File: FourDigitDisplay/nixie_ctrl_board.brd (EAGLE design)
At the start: 100 x 50 mm, 8 parts, among them Q1 IN-12B, Q2 IN-12B, Q3 IN-12B, Q4 IN-12B

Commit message: IC群を追加して仮置き
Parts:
- added CN1: PIC_CN_H, Connectors:HEADER_6PIN
- added CN2: I2C_IF, PartsForProto:I2C_IF_4PIN
- added R1, R2, R8, R9: 20k, Parts:RESISTOR_0207_300MIL
- added R11, R12, R3, R4: 470, Parts:RESISTOR_0207_300MIL
- added U1, U3: TLP627-2, Parts:DIL08
- added U2, U4: SN74141, Parts:DIL16
- added U5: PIC16F18857-I/SP, Parts:DIL28-3
- moved Q1 1.27 mm to (12.1, 26.7)
- moved Q2 1.27 mm to (37.5, 26.7)
- moved Q3 1.27 mm to (62.9, 26.7)
- moved Q4 1.27 mm to (88.3, 26.7)
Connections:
- new net +24V: R1.2, R2.2, R8.2, R9.2
- new net +5V: U2.5, U4.5
- new net 0V: U1.2, U1.4, U2.12, U3.2, U3.4, U4.12
- new net A1_CTL: R11.1
- new net A2_CTL: R12.1
- new net A3_CTL: R3.1
- new net A4_CTL: R4.1
- new net N$1: R1.1, U1.8
- new net N$11: R8.1, U3.8
- new net N$12: R9.1, U3.6
- new net N$13: R11.2, U3.1
- new net N$14: R12.2, U3.3
- new net N$2: R2.1, U1.6
- new net N$3: R3.2, U1.1
- new net N$4: R4.2, U1.3
- new net PIC_A1: U2.3
- new net PIC_A2: U4.3
- new net PIC_B1: U2.6
- new net PIC_B2: U4.6
- new net PIC_C1: U2.7
- new net PIC_C2: U4.7
- new net PIC_D1: U2.4
- new net PIC_D2: U4.4
- net A_1: now also U3.7
- net A_2: now also U3.5
- net A_3: now also U1.7
- net A_4: now also U1.5
- net K1_0: now also U2.16
- net K1_1: now also U2.15
- net K1_2: now also U2.8
- net K1_3: now also U2.9
- net K1_4: now also U2.13
- net K1_5: now also U2.14
- net K1_6: now also U2.11
- net K1_7: now also U2.10
- net K1_8: now also U2.1
- net K1_9: now also U2.2
- net K2_0: now also U4.16
- net K2_1: now also U4.15
- net K2_2: now also U4.8
- net K2_3: now also U4.9
- net K2_4: now also U4.13
- net K2_5: now also U4.14
- net K2_6: now also U4.11
- net K2_7: now also U4.10
- net K2_8: now also U4.1
- net K2_9: now also U4.2
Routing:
- added copper zone on layer 16, net 0V
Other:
- board size 100 x 50 mm -> 100 x 65 mm

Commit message: 配線の追加
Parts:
- added C1: 0.1uF, Parts:CAP_100MIL
- added CN3, CN4: POWER_IF, PartsForProto:HEADER_2PIN_POWER_IF
- added R5: 10k, Parts:RESISTOR_0207_300MIL
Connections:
- new net N$15: CN1.3, U5.8
- new net N$5: CN2.2, U5.15
- new net N$6: CN2.3, U5.14
- new net N$7: CN1.1, R5.1, U5.1
- new net N$8: CN1.4, U5.28
- new net N$9: CN1.5, U5.27
- net +24V: now also CN3.2
- net +5V: now also C1.1, CN1.2, CN2.4, CN4.2, R5.2, U5.20
- net 0V: now also C1.2, CN2.1, CN3.1, CN4.1, U5.19
- net A1_CTL: now also U5.6
- net A2_CTL: now also U5.7
- net A3_CTL: now also U5.25
- net A4_CTL: now also U5.26
- net K1_D: now also U5.11
- net K2_D: now also U5.12
- net PIC_A1: now also U5.2
- net PIC_A2: now also U5.21
- net PIC_B1: now also U5.3
- net PIC_B2: now also U5.22
- net PIC_C1: now also U5.4
- net PIC_C2: now also U5.23
- net PIC_D1: now also U5.5
- net PIC_D2: now also U5.24
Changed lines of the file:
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@@
 <element name="U4" library="Parts" package="DIL16" value="SN74141" x="77.47" y="52.07" rot="R270"/>
 <element name="U5" library="Parts" package="DIL28-3" value="PIC16F18857-I/SP" x="49.53" y="52.07"/>
+<element name="CN3" library="PartsForProto" package="HEADER_2PIN_POWER_IF" value="POWER_IF" x="-1.27" y="-7.62"/>
+<element name="CN4" library="PartsForProto" package="HEADER_2PIN_POWER_IF" value="POWER_IF" x="-1.27" y="-16.51"/>
+<element name="R5" library="Parts" package="RESISTOR_0207_300MIL" value="10k" x="-1.27" y="-25.4"/>
+<element name="C1" library="Parts" package="CAP_100MIL" value="0.1uF" x="-1.27" y="-29.21"/>
 </elements>
 <signals>
@@
 <contactref element="Q3" pad="12"/>
 <contactref element="Q4" pad="12"/>
-<wire x1="62.865" y1="17.67" x2="88.265" y2="17.67" width="0" layer="19" extent="1-1"/>
+<contactref element="U5" pad="12"/>
+<wire x1="62.865" y1="17.67" x2="60.96" y2="48.26" width="0" layer="19" extent="1-1"/>
+<wire x1="88.265" y1="17.67" x2="62.865" y2="17.67" width="0" layer="19" extent="1-1"/>
 </signal>
 <signal name="K1_1">
@@
 <contactref element="Q1" pad="12"/>
 <contactref element="Q2" pad="12"/>
+<contactref element="U5" pad="11"/>
+<wire x1="37.465" y1="17.67" x2="58.42" y2="48.26" width="0" layer="19" extent="1-1"/>
 <wire x1="12.065" y1="17.67" x2="37.465" y2="17.67" width="0" layer="19" extent="1-1"/>
 </signal>
@@
 <vertex x="-3.81" y="-3.81"/>
 </polygon>
+<contactref element="CN3" pad="1"/>
+<contactref element="CN4" pad="1"/>
+<contactref element="U5" pad="19"/>
+<contactref element="C1" pad="2"/>
+<contactref element="CN2" pad="1"/>
+<wire x1="55.88" y1="55.88" x2="81.28" y2="50.8" width="0" layer="19" extent="1-1"/>
+<wire x1="24.13" y1="52.07" x2="55.88" y2="55.88" width="0" layer="19" extent="1-1"/>
+<wire x1="3.81" y1="59.69" x2="24.13" y2="52.07" width="0" layer="19" extent="1-1"/>
+<wire x1="22.86" y1="7.62" x2="24.13" y2="52.07" width="0" layer="19" extent="1-1"/>
+<wire x1="22.86" y1="2.54" x2="22.86" y2="7.62" width="0" layer="19" extent="1-1"/>
+<wire x1="-1.27" y1="-7.62" x2="22.86" y2="2.54" width="0" layer="19" extent="1-1"/>
+<wire x1="-1.27" y1="-16.51" x2="-1.27" y2="-7.62" width="0" layer="19" extent="1-1"/>
+<wire x1="0" y1="-29.21" x2="-1.27" y2="-16.51" width="0" layer="19" extent="1-1"/>
+<wire x1="69.85" y1="7.62" x2="81.28" y2="50.8" width="0" layer="19" extent="1-1"/>
+<wire x1="69.85" y1="2.54" x2="69.85" y2="7.62" width="0" layer="19" extent="1-1"/>
 </signal>
 <signal name="+24V">
@@
 <contactref element="R1" pad="2"/>
 <contactref element="R2" pad="2"/>
+<contactref element="CN3" pad="2"/>
 <wire x1="90.17" y1="2.54" x2="90.17" y2="7.62" width="0" layer="19" extent="1-1"/>
 <wire x1="43.18" y1="7.62" x2="90.17" y2="7.62" width="0" layer="19" extent="1-1"/>
 <wire x1="43.18" y1="2.54" x2="43.18" y2="7.62" width="0" layer="19" extent="1-1"/>
+<wire x1="1.27" y1="-7.62" x2="43.18" y2="2.54" width="0" layer="19" extent="1-1"/>
 </signal>
 <signal name="PIC_A2">
 <contactref element="U4" pad="3"/>
+<contactref element="U5" pad="21"/>
+<wire x1="50.8" y1="55.88" x2="73.66" y2="55.88" width="0" layer="19" extent="1-1"/>
 </signal>
 <signal name="PIC_D2">
 <contactref element="U4" pad="4"/>
+<contactref element="U5" pad="24"/>
+<wire x1="43.18" y1="55.88" x2="73.66" y2="53.34" width="0" layer="19" extent="1-1"/>
 </signal>
 <signal name="PIC_B2">
 <contactref element="U4" pad="6"/>
+<contactref element="U5" pad="22"/>
+<wire x1="48.26" y1="55.88" x2="73.66" y2="48.26" width="0" layer="19" extent="1-1"/>
 </signal>
 <signal name="PIC_C2">
 <contactref element="U4" pad="7"/>
+<contactref element="U5" pad="23"/>
+<wire x1="45.72" y1="55.88" x2="73.66" y2="45.72" width="0" layer="19" extent="1-1"/>
 </signal>
 <signal name="+5V">
 <contactref element="U2" pad="5"/>
 <contactref element="U4" pad="5"/>
-<wire x1="16.51" y1="52.07" x2="73.66" y2="50.8" width="0" layer="19" extent="1-1"/>
+<contactref element="CN4" pad="2"/>
+<contactref element="CN1" pad="2"/>
+<contactref element="R5" pad="2"/>
+<contactref element="U5" pad="20"/>
+<contactref element="C1" pad="1"/>
+<contactref element="CN2" pad="4"/>
+<wire x1="57.15" y1="60.96" x2="73.66" y2="50.8" width="0" layer="19" extent="1-1"/>
+<wire x1="53.34" y1="55.88" x2="57.15" y2="60.96" width="0" layer="19" extent="1-1"/>
+<wire x1="16.51" y1="52.07" x2="53.34" y2="55.88" width="0" layer="19" extent="1-1"/>
+<wire x1="11.43" y1="59.69" x2="16.51" y2="52.07" width="0" layer="19" extent="1-1"/>
+<wire x1="1.27" y1="-16.51" x2="16.51" y2="52.07" width="0" layer="19" extent="1-1"/>
+<wire x1="6.35" y1="-25.4" x2="1.27" y2="-16.51" width="0" layer="19" extent="1-1"/>
+<wire x1="-2.54" y1="-29.21" x2="6.35" y2="-25.4" width="0" layer="19" extent="1-1"/>
 </signal>
 <signal name="N$11">
@@
 <signal name="A2_CTL">
 <contactref element="R12" pad="1"/>
+<contactref element="U5" pad="7"/>
+<wire x1="10.16" y1="2.54" x2="48.26" y2="48.26" width="0" layer="19" extent="1-1"/>
 </signal>
 <signal name="A1_CTL">
 <contactref element="R11" pad="1"/>
+<contactref element="U5" pad="6"/>
+<wire x1="10.16" y1="7.62" x2="45.72" y2="48.26" width="0" layer="19" extent="1-1"/>
 </signal>
 <signal name="N$1">
@@
 <signal name="A3_CTL">
 <contactref element="R3" pad="1"/>
+<contactref element="U5" pad="25"/>
+<wire x1="57.15" y1="7.62" x2="40.64" y2="55.88" width="0" layer="19" extent="1-1"/>
 </signal>
 <signal name="A4_CTL">
 <contactref element="R4" pad="1"/>
+<contactref element="U5" pad="26"/>
+<wire x1="57.15" y1="2.54" x2="38.1" y2="55.88" width="0" layer="19" extent="1-1"/>
 </signal>
 <signal name="PIC_A1">
 <contactref element="U2" pad="3"/>
+<contactref element="U5" pad="2"/>
+<wire x1="16.51" y1="57.15" x2="35.56" y2="48.26" width="0" layer="19" extent="1-1"/>
 </signal>
 <signal name="PIC_D1">
 <contactref element="U2" pad="4"/>
+<contactref element="U5" pad="5"/>
+<wire x1="16.51" y1="54.61" x2="43.18" y2="48.26" width="0" layer="19" extent="1-1"/>
 </signal>
 <signal name="PIC_B1">
 <contactref element="U2" pad="6"/>
+<contactref element="U5" pad="3"/>
+<wire x1="16.51" y1="49.53" x2="38.1" y2="48.26" width="0" layer="19" extent="1-1"/>
 </signal>
 <signal name="PIC_C1">
 <contactref element="U2" pad="7"/>
+<contactref element="U5" pad="4"/>
+<wire x1="16.51" y1="46.99" x2="40.64" y2="48.26" width="0" layer="19" extent="1-1"/>
+</signal>
+<signal name="N$7">
+<contactref element="CN1" pad="1"/>
+<contactref element="U5" pad="1"/>
+<contactref element="R5" pad="1"/>
+<wire x1="33.02" y1="48.26" x2="54.61" y2="60.96" width="0" layer="19" extent="1-1"/>
+<wire x1="-1.27" y1="-25.4" x2="33.02" y2="48.26" width="0" layer="19" extent="1-1"/>
+</signal>
+<signal name="N$8">
+<contactref element="CN1" pad="4"/>
+<contactref element="U5" pad="28"/>
+<wire x1="33.02" y1="55.88" x2="62.23" y2="60.96" width="0" layer="19" extent="1-1"/>
+</signal>
+<signal name="N$9">
+<contactref element="U5" pad="27"/>
+<contactref element="CN1" pad="5"/>
+<wire x1="35.56" y1="55.88" x2="64.77" y2="60.96" width="0" layer="19" extent="1-1"/>
+</signal>
+<signal name="N$15">
+<contactref element="U5" pad="8"/>
+<contactref element="CN1" pad="3"/>
+<wire x1="50.8" y1="48.26" x2="59.69" y2="60.96" width="0" layer="19" extent="1-1"/>
+</signal>
+<signal name="N$5">
+<contactref element="U5" pad="15"/>
+<contactref element="CN2" pad="2"/>
+<wire x1="6.35" y1="59.69" x2="66.04" y2="55.88" width="0" layer="19" extent="1-1"/>
+</signal>
+<signal name="N$6">
+<contactref element="CN2" pad="3"/>
+<contactref element="U5" pad="14"/>
+<wire x1="8.89" y1="59.69" x2="66.04" y2="48.26" width="0" layer="19" extent="1-1"/>
 </signal>
 </signals>

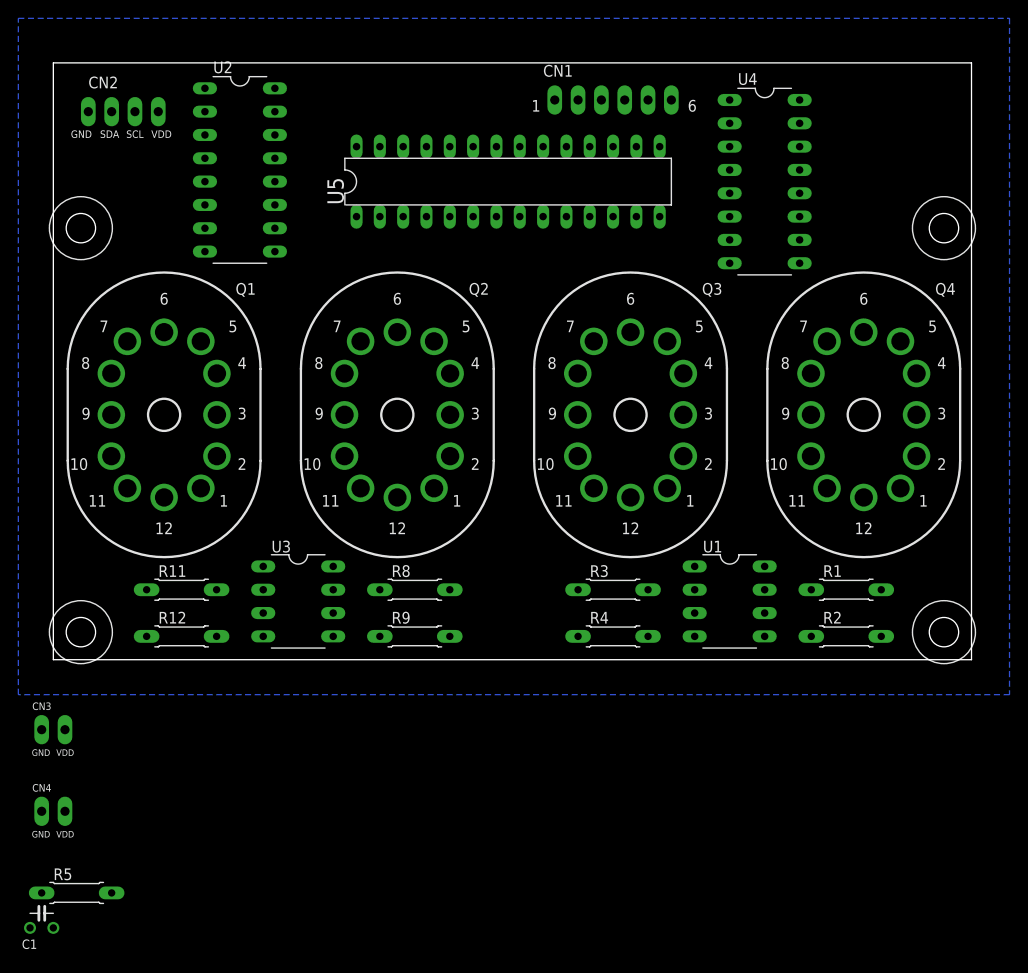
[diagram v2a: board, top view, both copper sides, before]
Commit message: 部品配置修正
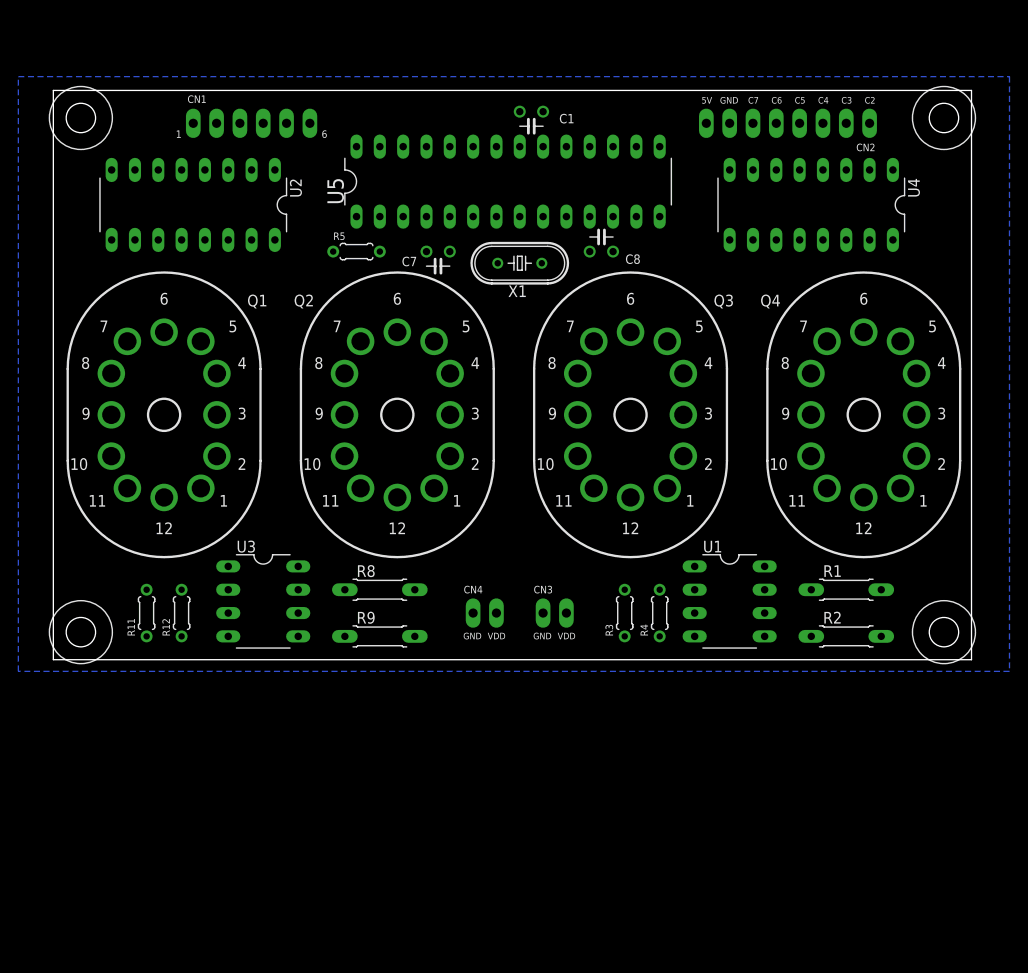
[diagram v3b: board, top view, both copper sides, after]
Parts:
- added C7, C8: 22pF, Parts:CAP_100MIL
- added X1: 20MHz, Parts:HC-49/S
- CN2: value I2C_IF -> PIC_NIXIE_IF; device PartsForProto:I2C_IF_4PIN -> PartsForProto:PIC_IF_NIXIE_8PIN
- R11, R12, R3, R4, R5: device Parts:RESISTOR_0207_300MIL -> Parts:RESISTOR_0204_200MIL
- moved C1 103.7 mm to (52.1, 59.7), turned to 180 degrees
- moved CN2 85.1 mm to (88.9, 58.4), turned to 180 degrees
- moved R5 77.8 mm to (33.0, 44.5)
- moved CN3 56.1 mm to (53.3, 5.08)
- moved CN4 51.7 mm to (45.7, 5.08)
- moved CN1 39.5 mm to (15.2, 58.4)
- moved H2 12.0 mm to (3.00, 59.0)
- moved H3 12.0 mm to (97.0, 59.0)
- moved R4 9.25 mm to (66.0, 5.08), turned to 90 degrees
- moved U2 6.35 mm to (15.2, 49.5), turned to 180 degrees
- moved R3 5.68 mm to (62.2, 5.08), turned to 90 degrees
- moved U4 5.68 mm to (82.5, 49.5), turned to 180 degrees
- moved R12 4.58 mm to (14.0, 5.08), turned to 90 degrees
- moved R8 3.81 mm to (31.8, 7.62)
- moved R9 3.81 mm to (31.8, 2.54)
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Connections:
- new net N$10: CN2.4, U5.16
- new net N$16: CN2.3, U5.15
- new net N$17: CN2.2, U5.14
- new net N$18: CN2.1, U5.13
- new net OSC1: C7.1, U5.9, X1.1
- new net OSC2: C8.1, U5.10, X1.2
- net +5V: now also CN2.8; no longer CN2.4
- net 0V: now also C7.2, C8.2, CN2.7; no longer CN2.1
- net N$5: now also CN2.6, U5.18; no longer CN2.2, U5.15
- net N$6: now also CN2.5, U5.17; no longer CN2.3, U5.14
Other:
- board size 100 x 65 mm -> 100 x 62 mm
